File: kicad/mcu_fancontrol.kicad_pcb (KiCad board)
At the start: 2 copper layers, 60 x 32 mm, 51 parts, among them J1 Vin, J10 Output2, J11 NTC2, J2 I2C, J3 I2C, J4 1-Wire, J5 1-Wire, J6 SWIM, J7 UART, J8 NTC1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

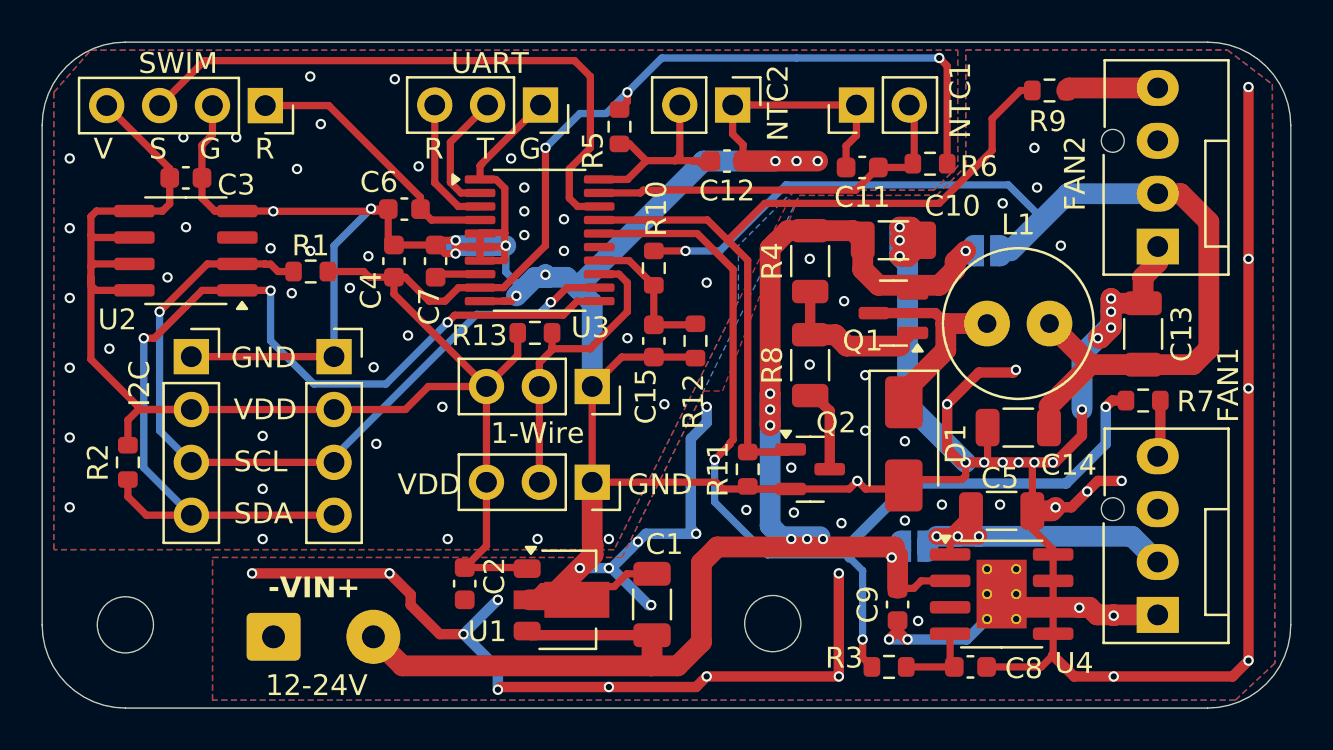
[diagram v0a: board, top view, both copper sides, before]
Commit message: pcb: Add teadrops, round tracks
Other minor fixes
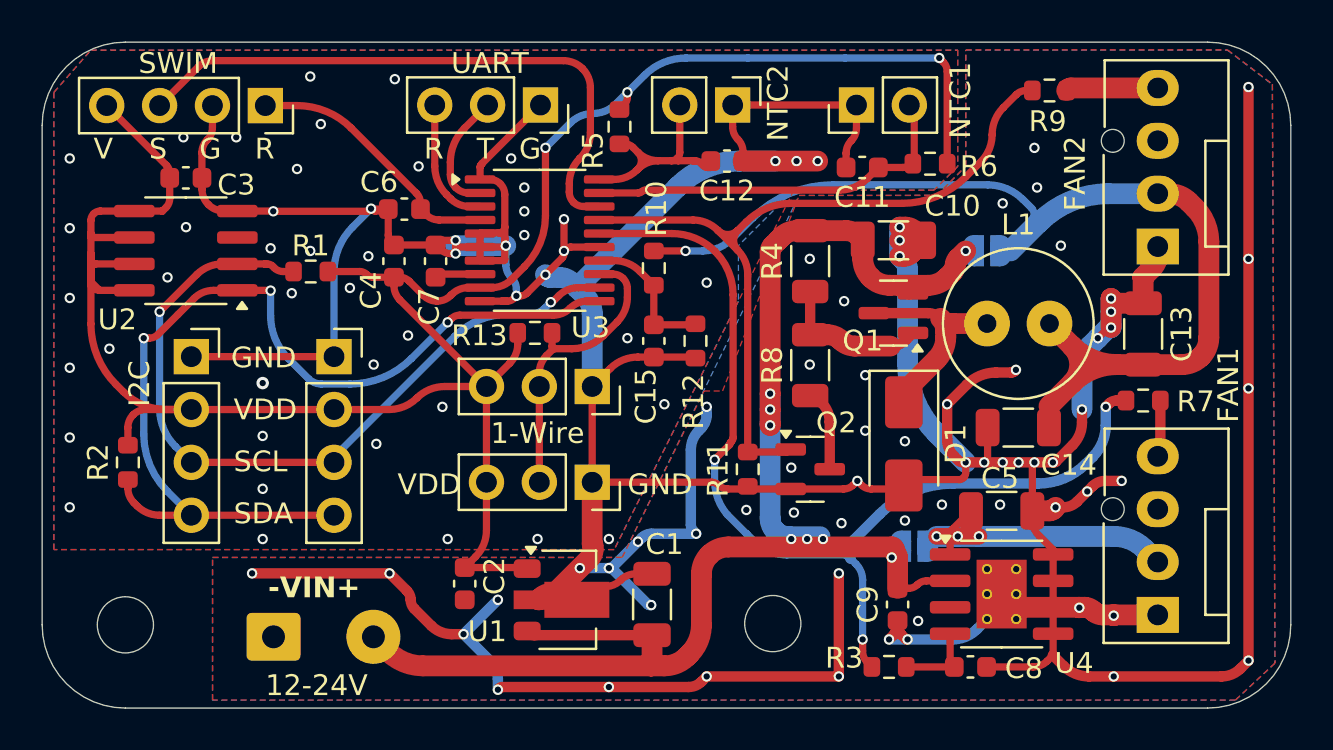
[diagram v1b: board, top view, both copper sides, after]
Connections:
- U3 pad 15: unconnected-(U3-PC5-Pad15) -> GND
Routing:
- net GND: track 309.7 -> 313.1 mm, vias 112 -> 113
- net /PWMP2: track 51.8 -> 53.5 mm
- net /NTC2: track 10.3 -> 11.7 mm
- net /V5_33: track 114.9 -> 116.2 mm
- net /PWM1: track 49.8 -> 48.8 mm
- net /SDA: track 48.3 -> 47.4 mm
- net Net-(D1-K): track 9.98 -> 10.7 mm
- net /PWM2: track 37.8 -> 38.4 mm
- net /SCL: track 38.7 -> 38.1 mm
- net /V12_24: track 75.6 -> 75.0 mm
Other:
- board text added: "2ch Fan Controller v2"
- board text removed: "2CH Fan controller"
